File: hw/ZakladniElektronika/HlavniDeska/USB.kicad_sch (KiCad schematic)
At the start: 19 parts, among them J2 USB_C_Receptacle_USB2.0, U2 TPD4E02B04DQA, U4 AP33772

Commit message: WIP
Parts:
- C137, C139, C140: Basic/Extended E -> B; LCSC C131394 -> C307331; info (none) -> 50V, X7R
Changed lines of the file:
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@@
       (effects (font (size 1.27 1.27)) hide)
     )
-    (property "LCSC" "C131394" (at 184.15 81.28 0)
-      (effects (font (size 1.27 1.27)) hide)
-    )
-    (property "Basic/Extended" "E" (at 184.15 81.28 0)
+    (property "LCSC" "C307331" (at 184.15 81.28 0)
+      (effects (font (size 1.27 1.27)) hide)
+    )
+    (property "Basic/Extended" "B" (at 184.15 81.28 0)
+      (effects (font (size 1.27 1.27)) hide)
+    )
+    (property "info" "50V, X7R" (at 184.15 81.28 0)
       (effects (font (size 1.27 1.27)) hide)
     )
@@
       (effects (font (size 1.27 1.27)) hide)
     )
-    (property "LCSC" "C131394" (at 220.98 118.11 0)
-      (effects (font (size 1.27 1.27)) hide)
-    )
-    (property "Basic/Extended" "E" (at 220.98 118.11 0)
+    (property "LCSC" "C307331" (at 220.98 118.11 0)
+      (effects (font (size 1.27 1.27)) hide)
+    )
+    (property "Basic/Extended" "B" (at 220.98 118.11 0)
+      (effects (font (size 1.27 1.27)) hide)
+    )
+    (property "info" "50V, X7R" (at 220.98 118.11 0)
       (effects (font (size 1.27 1.27)) hide)
     )
@@
       (effects (font (size 1.27 1.27)) hide)
     )
-    (property "LCSC" "C131394" (at 190.5 118.11 0)
-      (effects (font (size 1.27 1.27)) hide)
-    )
-    (property "Basic/Extended" "E" (at 190.5 118.11 0)
-      (effects (font (size 1.27 1.27)) hide)
-    )
+    (property "LCSC" "C307331" (at 190.5 118.11 0)
+      (effects (font (size 1.27 1.27)) hide)
+    )
+    (property "Basic/Extended" "B" (at 190.5 118.11 0)
+      (effects (font (size 1.27 1.27)) hide)
+    )
+    (property "info" "50V, X7R" (at 190.5 118.11 0)
+      (effects (font (size 1.27 1.27)) hide)
+    )

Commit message: Nastin schematu
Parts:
- renumbered D126 to LED, D125 to LED
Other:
- note added: "PD jednatel"
- note added: "USB s ESD ochranou"
- note removed: "PD sink"
- note removed: "USB to ESP"
- moved on the sheet: C136, C137, C138, C139, C140, C141, LED, R11, R12, R13, R3, R4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

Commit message: Zaciame psat
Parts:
- removed D121: ${SIM.PARAMS}, Diode_SMD:D_SMA, symbol Device:D
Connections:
- net GND: now also J2.S1 (SHIELD)
- net VUSB: no longer C136.1, C137.1, D123.3 (K), LED.2 (A), R11.1, U4.1 (ISENP)
- net V_USB: now reaches J2.A4 (VBUS), J2.A9 (VBUS), J2.B4 (VBUS), J2.B9 (VBUS)
- net V_USB: now also C136.1, C137.1, D123.3 (K), LED.2 (A), R11.1, U4.1 (ISENP)
- no-connect marks 8 -> 7
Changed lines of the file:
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@@
   (no_connect (at 220.98 100.33))
   (no_connect (at 220.98 110.49))
-  (no_connect (at 63.5 105.41))
   (no_connect (at 86.36 95.25))
   (no_connect (at 86.36 97.79))
@@
     (stroke (width 0) (type default))
   )
-  (wire (pts (xy 86.36 67.31) (xy 88.9 67.31))
+  (wire (pts (xy 86.36 67.31) (xy 99.06 67.31))
     (stroke (width 0) (type default))
   )
@@
     (stroke (width 0) (type default))
   )
-  (wire (pts (xy 115.57 64.77) (xy 115.57 67.31))
-    (stroke (width 0) (type default))
-  )
   (wire (pts (xy 180.34 67.31) (xy 180.34 81.28))
     (stroke (width 0) (type default))
@@
   )
   (wire (pts (xy 88.9 85.09) (xy 101.6 85.09))
-    (stroke (width 0) (type default))
-  )
-  (wire (pts (xy 99.06 67.31) (xy 96.52 67.31))
     (stroke (width 0) (type default))
   )
@@
     (effects (font (size 1.27 1.27)) (justify right))
   )
+  (hierarchical_label "GND" (shape input) (at 63.5 105.41 270) (fields_autoplaced)
+    (effects (font (size 1.27 1.27)) (justify right))
+  )
   (hierarchical_label "GND" (shape input) (at 167.64 85.09 270) (fields_autoplaced)
     (effects (font (size 1.27 1.27)) (justify right))
@@
   (hierarchical_label "GND" (shape input) (at 193.04 121.92 270) (fields_autoplaced)
     (effects (font (size 1.27 1.27)) (justify right))
-  )
-  (hierarchical_label "VUSB" (shape output) (at 115.57 64.77 90) (fields_autoplaced)
-    (effects (font (size 1.27 1.27)) (justify left))
   )
   (hierarchical_label "GND" (shape input) (at 208.28 121.92 270) (fields_autoplaced)
@@
         )
       )
-    )
-  )
-  (symbol (lib_id "Device:D") (at 92.71 67.31 0) (mirror y) (unit 1)
-    (in_bom yes) (on_board yes) (dnp no)
-    (property "Reference" "D121" (at 92.71 63.5 0)
-      (effects (font (size 1.27 1.27)))
-    )
-    (property "Value" "${SIM.PARAMS}" (at 92.71 64.77 0)
-      (effects (font (size 1.27 1.27)) hide)
-    )
-    (property "Footprint" "Diode_SMD:D_SMA" (at 92.71 67.31 0)
-      (effects (font (size 1.27 1.27)) hide)
-    )
-    (property "Datasheet" "~" (at 92.71 67.31 0)
-      (effects (font (size 1.27 1.27)) hide)
-    )
-    (property "LCSC" "C8678" (at 92.71 67.31 0)
-      (effects (font (size 1.27 1.27)) hide)
-    )
-    (property "JLCPCB_CORRECTION" "0;0;0" (at 92.71 67.31 0)
-      (effects (font (size 1.27 1.27)) hide)
-    )
-    (property "Sim.Device" "SPICE" (at 92.71 67.31 0)
-      (effects (font (size 1.27 1.27)) (justify left) hide)
-    )
-    (property "Sim.Params" "type=\"D\" model=\"DIODE\" lib=\"\"" (at 12.7 25.4 0)
-      (effects (font (size 1.27 1.27)) hide)
-    )
-    (property "Sim.Pins" "1=1 2=2" (at 12.7 25.4 0)
-      (effects (font (size 1.27 1.27)) hide)
-    )
-    (pin "1")
-    (pin "2")
-    (instances
-      (project "ZakladniElektronika"
-        (path "/99cd3e15-4eb6-4cbb-8726-789aedd3df15/c3b70d9b-0dcb-4344-9507-13ff5b4c000e/2f609c37-b91c-437d-a066-c26014011f90"
-          (reference "D121") (unit 1)
-        )
-      )
-      (project "RB3203"
-        (path "/dc7f8a41-3453-4df6-94dc-e94521e89591/9c917b4f-c6c7-4191-9aaa-f982c264da50/42c6643c-04e2-43ad-8f0e-80e5d3fe214b"
-          (reference "D?") (unit 1)
-        )
-      )

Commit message: Zavazbení zapínání
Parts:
- renumbered LED to LED3, LED to LED4
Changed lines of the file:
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@@
   (symbol (lib_id "Device:LED") (at 241.3 110.49 90) (unit 1)
     (in_bom yes) (on_board yes) (dnp no)
-    (property "Reference" "LED" (at 243.84 109.22 90)
+    (property "Reference" "LED4" (at 243.84 109.22 90)
       (effects (font (size 1.27 1.27)) (justify right))
     )
@@
       (project "ZakladniElektronika"
         (path "/99cd3e15-4eb6-4cbb-8726-789aedd3df15/c3b70d9b-0dcb-4344-9507-13ff5b4c000e/2f609c37-b91c-437d-a066-c26014011f90"
-          (reference "LED") (unit 1)
+          (reference "LED4") (unit 1)
         )
       )
@@
   (symbol (lib_id "Device:LED") (at 167.64 73.66 90) (unit 1)
     (in_bom yes) (on_board yes) (dnp no)
-    (property "Reference" "LED" (at 170.18 72.39 90)
+    (property "Reference" "LED3" (at 170.18 72.39 90)
       (effects (font (size 1.27 1.27)) (justify right))
     )
@@
       (project "ZakladniElektronika"
         (path "/99cd3e15-4eb6-4cbb-8726-789aedd3df15/c3b70d9b-0dcb-4344-9507-13ff5b4c000e/2f609c37-b91c-437d-a066-c26014011f90"
-          (reference "LED") (unit 1)
-        )
-      )
+          (reference "LED3") (unit 1)
+        )
+      )

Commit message: USB_multiplexer a přehlednost
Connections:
- net D+_ESP renamed D+
- net D-_ESP renamed D-
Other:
- moved on the sheet: C138

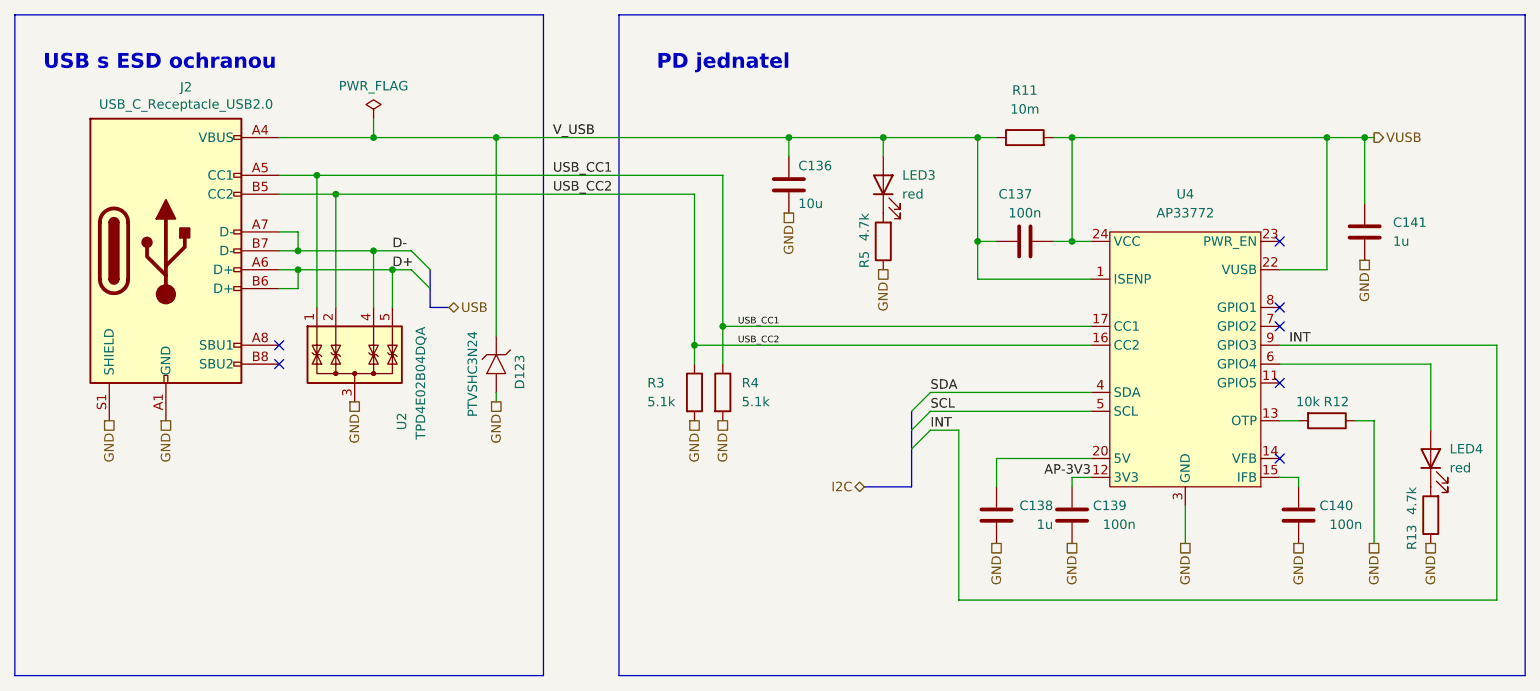
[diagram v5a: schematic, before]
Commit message: Likvidace MiniUI jako samostatné desky a výběr všech komponent
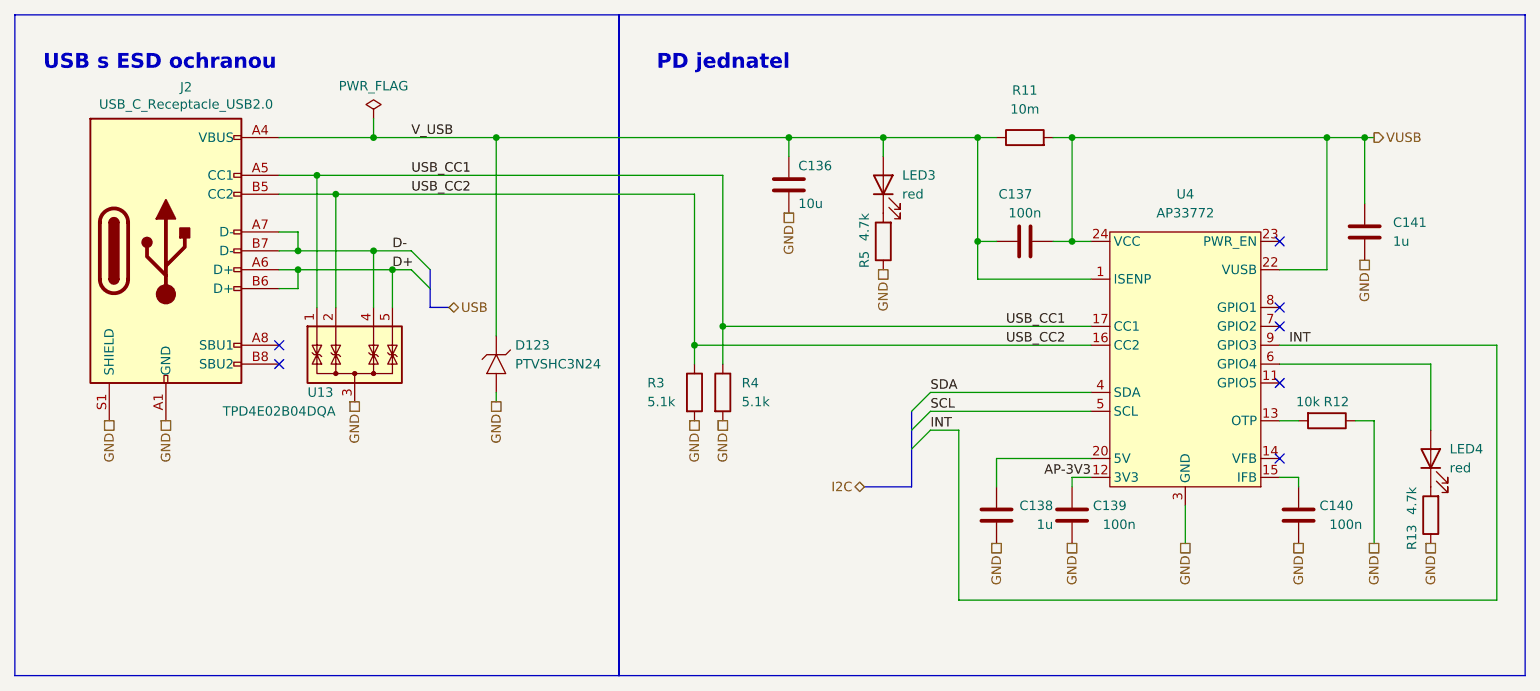
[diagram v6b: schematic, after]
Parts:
- removed U2: TPD4E02B04DQA, Package_SON:USON-10_2.5x1.0mm_P0.5mm, symbol Power_Protection:TPD4E02B04DQA
- added U13: TPD4E02B04DQA, Package_SON:USON-10_2.5x1.0mm_P0.5mm, symbol RKL-Uncategorized:TPD4E02B04DQA
- C136: footprint Capacitor_SMD:C_0603_1608Metric -> Capacitor_SMD:C_0805_2012Metric; LCSC C96446 -> C440198; info (none) -> 50V, X5R
- C138, C141: footprint Resistor_SMD:R_0402_1005Metric -> Capacitor_SMD:C_0402_1005Metric; Basic/Extended B -> E; JLCPCB_CORRECTION (none) -> 0;0;0; LCSC C52923 -> C1518208; info (none) -> 50V, X5R (potenciálně C52923 což je 25V, X5R )
- D123: footprint Robotarna_KiCad_Library:DFN3-2x2 -> RKL-StandardPackages:DFN3-2x2; Basic/Extended (none) -> E
- J2: footprint Connector_USB:USB_C_Receptacle_HRO_TYPE-C-31-M-12 -> RKL-Connectors:USB31-TYPEC-33141-2FS; Basic/Extended (none) -> E; LCSC C165948 -> C480368
- R11: Basic/Extended (none) -> E
- R12: footprint Capacitor_SMD:C_0201_0603Metric -> Resistor_SMD:R_0402_1005Metric; Basic/Extended E -> B; JLCPCB_CORRECTION (none) -> 0;0;0; LCSC C106225 -> C25744
- R13, R5: footprint Resistor_SMD:R_0201_0603Metric -> Resistor_SMD:R_0402_1005Metric; Basic/Extended E -> B; LCSC C270346 -> C25900
- U4: Basic/Extended (none) -> No JLCPCB part; LCSC C5244513 -> (none)
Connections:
- net D+: now also U13.5 (IO4)
- net D-: now also U13.4 (IO3)
- net GND: now also U13.3 (G), U13.8 (G)
- net USB_CC1: now also U13.1 (IO1)
- net USB_CC2: now also U13.2 (IO2)

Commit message: Výmněna ochrany baterie
Předchozí ochranný čip JLCPCB nemělo na skladě
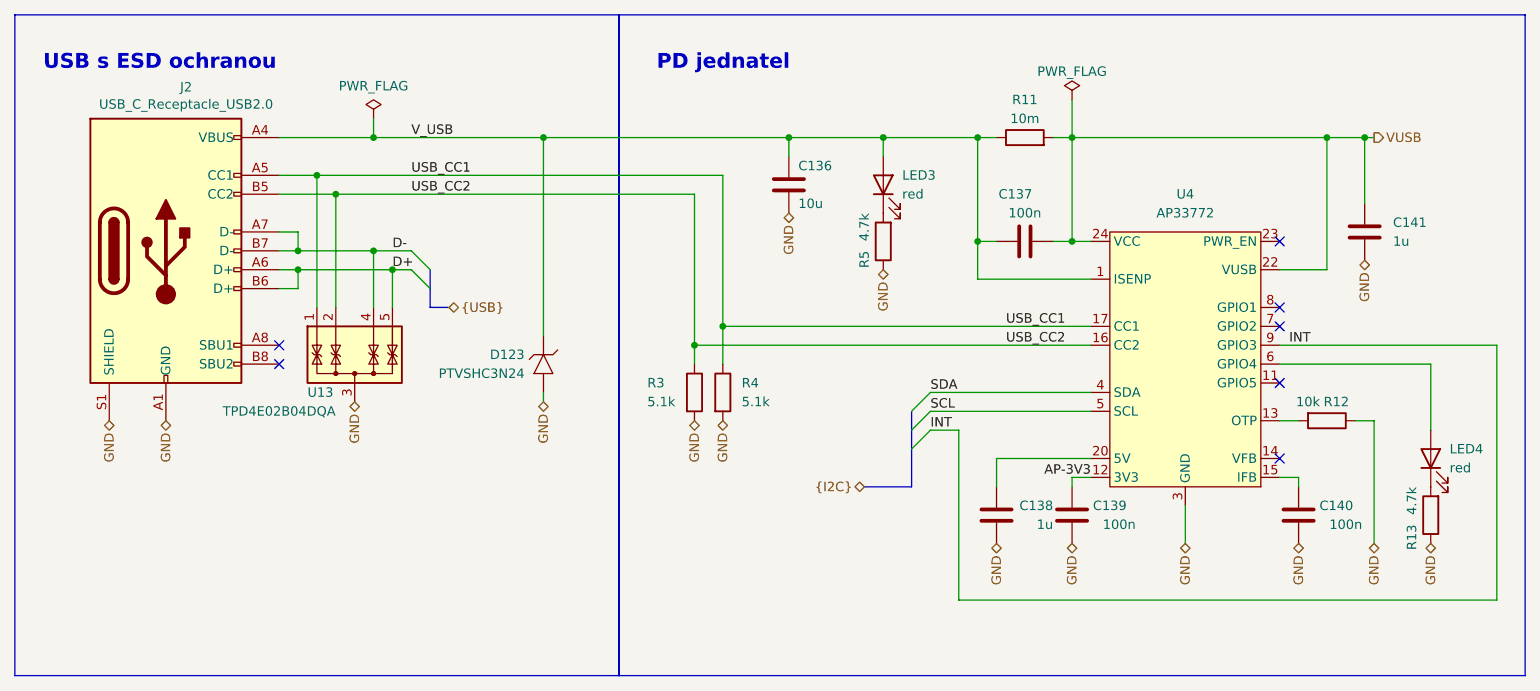
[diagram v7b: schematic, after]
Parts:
- D123: symbol Robotarna_KiCad_Library:PTVSHC3N24 -> RKL-Uncategorized:PTVSHC3N24
- U4: symbol RBCX:AP33772 -> RKL-BusCnverters:AP33772
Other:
- moved on the sheet: D123

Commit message: WIP
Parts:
- J2: symbol Connector:USB_C_Receptacle_USB2.0 -> Connector:USB_C_Receptacle
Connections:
- no-connect marks 7 -> 15
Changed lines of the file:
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@@
   )
   (no_connect (at 220.98 100.33))
+  (no_connect (at 86.36 107.95))
   (no_connect (at 220.98 110.49))
+  (no_connect (at 86.36 123.19))
+  (no_connect (at 86.36 100.33))
+  (no_connect (at 86.36 115.57))
+  (no_connect (at 86.36 125.73))
+  (no_connect (at 86.36 102.87))
   (no_connect (at 86.36 95.25))
-  (no_connect (at 86.36 97.79))
+  (no_connect (at 86.36 92.71))
+  (no_connect (at 86.36 110.49))
+  (no_connect (at 86.36 118.11))
   (no_connect (at 220.98 81.28))
   (no_connect (at 220.98 90.17))
@@
     (effects (font (size 1.27 1.27)) (justify right))
   )
-  (hierarchical_label "GND" (shape bidirectional) (at 71.12 105.41 270) (fields_autoplaced)
-    (effects (font (size 1.27 1.27)) (justify right))
-  )
-  (hierarchical_label "GND" (shape bidirectional) (at 63.5 105.41 270) (fields_autoplaced)
+  (hierarchical_label "GND" (shape bidirectional) (at 71.12 133.35 270) (fields_autoplaced)
+    (effects (font (size 1.27 1.27)) (justify right))
+  )
+  (hierarchical_label "GND" (shape bidirectional) (at 63.5 133.35 270) (fields_autoplaced)
     (effects (font (size 1.27 1.27)) (justify right))
   )
@@
     )
   )
-  (symbol (lib_id "Connector:USB_C_Receptacle_USB2.0") (at 71.12 82.55 0) (unit 1)
-    (in_bom yes) (on_board yes) (dnp no)
-    (property "Reference" "J2" (at 73.8378 60.5282 0)
+  (symbol (lib_id "Connector:USB_C_Receptacle") (at 71.12 92.71 0) (unit 1)
+    (in_bom yes) (on_board yes) (dnp no)
+    (property "Reference" "J2" (at 71.12 60.96 0)
       (effects (font (size 1.27 1.27)))
     )
@@
       (effects (font (size 1.27 1.27)))
     )
-    (property "Footprint" "RKL-Connectors:USB31-TYPEC-33141-2FS" (at 74.93 82.55 0)
-      (effects (font (size 1.27 1.27)) hide)
-    )
-    (property "Datasheet" "https://www.usb.org/sites/default/files/documents/usb_type-c.zip" (at 74.93 82.55 0)
-      (effects (font (size 1.27 1.27)) hide)
-    )
-    (property "LCSC" "C480368" (at 71.12 82.55 0)
-      (effects (font (size 1.27 1.27)) hide)
-    )
-    (property "JLCPCB_CORRECTION" "0;-1;0" (at 71.12 82.55 0)
-      (effects (font (size 1.27 1.27)) hide)
-    )
-    (property "Basic/Extended" "E" (at 71.12 82.55 0)
+    (property "Footprint" "RKL-Connectors:USB31-TYPEC-33141-2FS" (at 74.93 92.71 0)
+      (effects (font (size 1.27 1.27)) hide)
+    )
+    (property "Datasheet" "https://www.usb.org/sites/default/files/documents/usb_type-c.zip" (at 74.93 92.71 0)
+      (effects (font (size 1.27 1.27)) hide)
+    )
+    (property "LCSC" "C480368" (at 71.12 63.5 0)
+      (effects (font (size 1.27 1.27)) hide)
+    )
+    (property "JLCPCB_CORRECTION" "0;-1;0" (at 71.12 58.42 0)
+      (effects (font (size 1.27 1.27)) hide)
+    )
+    (property "Basic/Extended" "E" (at 71.12 60.96 0)
       (effects (font (size 1.27 1.27)) hide)
     )
     (pin "A1")
+    (pin "A10")
+    (pin "A11")
     (pin "A12")
+    (pin "A2")
+    (pin "A3")
     (pin "A4")
     (pin "A5")
@@
     (pin "A9")
     (pin "B1")
+    (pin "B10")
+    (pin "B11")
     (pin "B12")
+    (pin "B2")
+    (pin "B3")
     (pin "B4")
     (pin "B5")
@@
   (symbol (lib_id "RKL-Uncategorized:TPD4E02B04DQA") (at 96.52 92.71 0) (unit 1)
     (in_bom yes) (on_board yes) (dnp no)
-    (property "Reference" "U13" (at 90.17 101.6 0)
-      (effects (font (size 1.27 1.27)) (justify left))
-    )
-    (property "Value" "TPD4E02B04DQA" (at 86.36 104.14 0)
-      (effects (font (size 1.27 1.27)))
+    (property "Reference" "U13" (at 97.79 102.87 0)
+      (effects (font (size 1.27 1.27)) (justify left))
+    )
+    (property "Value" "TPD4E02B04DQA" (at 97.79 105.41 0)
+      (effects (font (size 1.27 1.27)) (justify left))
     )
     (property "Footprint" "Package_SON:USON-10_2.5x1.0mm_P0.5mm" (at 96.52 92.71 0)
